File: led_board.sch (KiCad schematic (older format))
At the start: 12 parts, among them J1 Conn_Coaxial, J2 Conn_Coaxial, J3 Conn_Coaxial, J4 Conn_Coaxial

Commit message: edits
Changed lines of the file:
@@
 Wire Wire Line
 	3000 3200 1500 3200
+$Comp
+L power:GND #PWR?
+U 1 1 5E6218D4
+P 3850 1950
+F 0 "#PWR?" H 3850 1700 50  0001 C CNN
+F 1 "GND" H 3855 1777 50  0000 C CNN
+F 2 "" H 3850 1950 50  0001 C CNN
+F 3 "" H 3850 1950 50  0001 C CNN
+	1    3850 1950
+	1    0    0    -1
+$EndComp
+Wire Wire Line
+	3850 1950 3850 1750
+Wire Wire Line
+	3850 1750 4000 1750
+Wire Wire Line
+	4000 1750 4000 1950
+Wire Wire Line
+	4000 1950 3850 1950
+Connection ~ 3850 1950
 $EndSCHEMATC

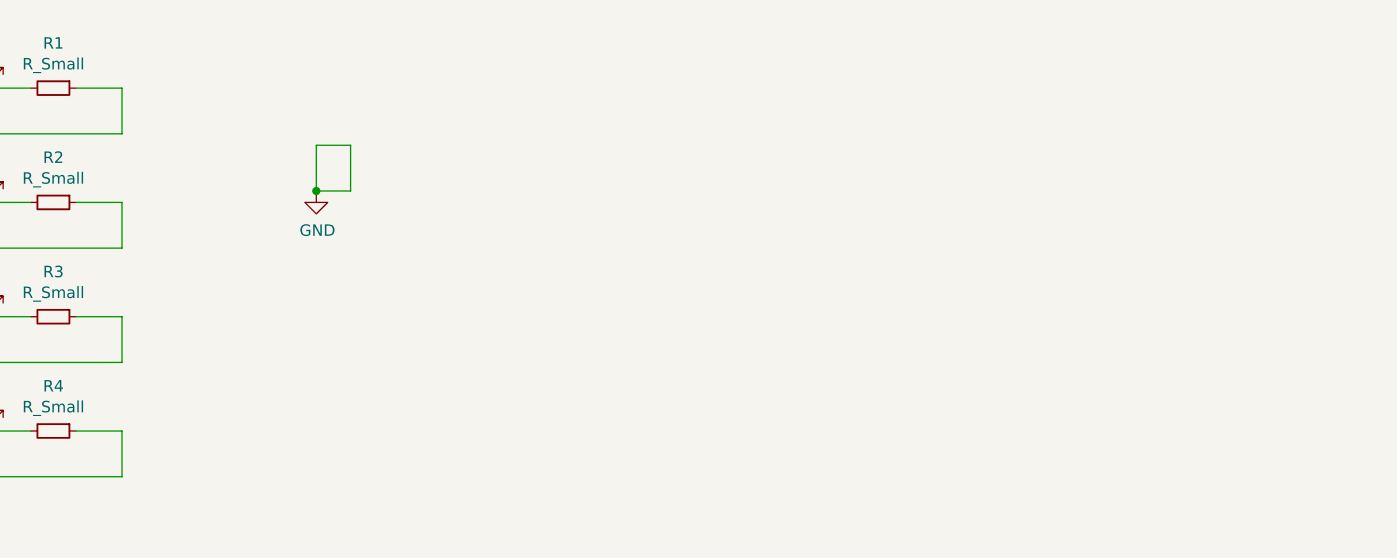
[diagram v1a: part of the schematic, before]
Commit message: rework for thorlabs 30mm cage
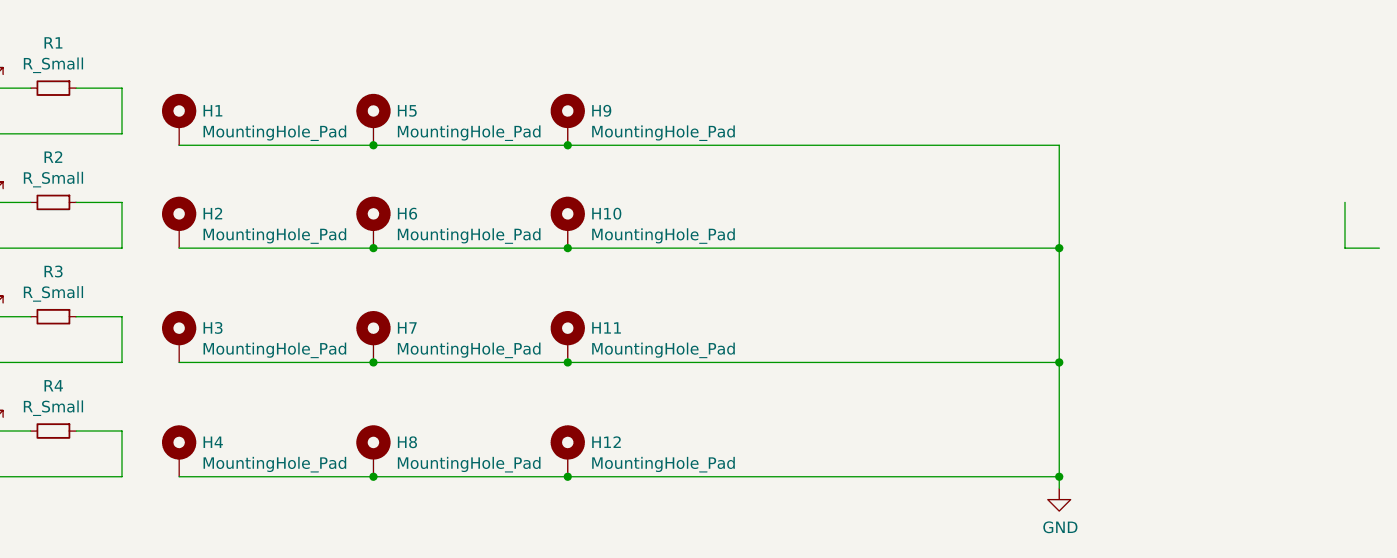
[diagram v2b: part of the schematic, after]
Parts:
- added H1, H10, H11, H12, H2, H3, H4, H5, H6, H7, H8, H9: MountingHole_Pad, MountingHole:MountingHole_6mm_Pad_Via, symbol Mechanical:MountingHole_Pad
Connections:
- wire segments 24 -> 38
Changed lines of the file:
@@
 	3000 3200 1500 3200
 $Comp
-L power:GND #PWR?
+L power:GND #PWR0101
 U 1 1 5E6218D4
-P 3850 1950
-F 0 "#PWR?" H 3850 1700 50  0001 C CNN
-F 1 "GND" H 3855 1777 50  0000 C CNN
-F 2 "" H 3850 1950 50  0001 C CNN
-F 3 "" H 3850 1950 50  0001 C CNN
-	1    3850 1950
+P 7100 3250
+F 0 "#PWR0101" H 7100 3000 50  0001 C CNN
+F 1 "GND" H 7105 3077 50  0000 C CNN
+F 2 "" H 7100 3250 50  0001 C CNN
+F 3 "" H 7100 3250 50  0001 C CNN
+	1    7100 3250
 	1    0    0    -1
 $EndComp
 Wire Wire Line
-	3850 1950 3850 1750
+	8350 2200 8350 2000
 Wire Wire Line
-	3850 1750 4000 1750
+	8500 2200 8350 2200
+$Comp
+L Mechanical:MountingHole_Pad H1
+U 1 1 5E61B0AD
+P 3250 1650
+F 0 "H1" H 3350 1699 50  0000 L CNN
+F 1 "MountingHole_Pad" H 3350 1608 50  0000 L CNN
+F 2 "MountingHole:MountingHole_6mm_Pad_Via" H 3250 1650 50  0001 C CNN
+F 3 "~" H 3250 1650 50  0001 C CNN
+	1    3250 1650
+	1    0    0    -1
+$EndComp
+$Comp
+L Mechanical:MountingHole_Pad H5
+U 1 1 5E61C87A
+P 4100 1650
+F 0 "H5" H 4200 1699 50  0000 L CNN
+F 1 "MountingHole_Pad" H 4200 1608 50  0000 L CNN
+F 2 "MountingHole:MountingHole_6mm_Pad_Via" H 4100 1650 50  0001 C CNN
+F 3 "~" H 4100 1650 50  0001 C CNN
+	1    4100 1650
+	1    0    0    -1
+$EndComp
+$Comp
+L Mechanical:MountingHole_Pad H9
+U 1 1 5E61CDCB
+P 4950 1650
+F 0 "H9" H 5050 1699 50  0000 L CNN
+F 1 "MountingHole_Pad" H 5050 1608 50  0000 L CNN
+F 2 "MountingHole:MountingHole_6mm_Pad_Via" H 4950 1650 50  0001 C CNN
+F 3 "~" H 4950 1650 50  0001 C CNN
+	1    4950 1650
+	1    0    0    -1
+$EndComp
+$Comp
+L Mechanical:MountingHole_Pad H2
+U 1 1 5E627D57
+P 3250 2100
+F 0 "H2" H 3350 2149 50  0000 L CNN
+F 1 "MountingHole_Pad" H 3350 2058 50  0000 L CNN
+F 2 "MountingHole:MountingHole_6mm_Pad_Via" H 3250 2100 50  0001 C CNN
+F 3 "~" H 3250 2100 50  0001 C CNN
+	1    3250 2100
+	1    0    0    -1
+$EndComp
+$Comp
+L Mechanical:MountingHole_Pad H6
+U 1 1 5E627D5D
+P 4100 2100
+F 0 "H6" H 4200 2149 50  0000 L CNN
+F 1 "MountingHole_Pad" H 4200 2058 50  0000 L CNN
+F 2 "MountingHole:MountingHole_6mm_Pad_Via" H 4100 2100 50  0001 C CNN
+F 3 "~" H 4100 2100 50  0001 C CNN
+	1    4100 2100
+	1    0    0    -1
+$EndComp
+$Comp
+L Mechanical:MountingHole_Pad H10
+U 1 1 5E627D63
+P 4950 2100
+F 0 "H10" H 5050 2149 50  0000 L CNN
+F 1 "MountingHole_Pad" H 5050 2058 50  0000 L CNN
+F 2 "MountingHole:MountingHole_6mm_Pad_Via" H 4950 2100 50  0001 C CNN
+F 3 "~" H 4950 2100 50  0001 C CNN
+	1    4950 2100
+	1    0    0    -1
+$EndComp
+$Comp
+L Mechanical:MountingHole_Pad H3
+U 1 1 5E628ADF
+P 3250 2600
+F 0 "H3" H 3350 2649 50  0000 L CNN
+F 1 "MountingHole_Pad" H 3350 2558 50  0000 L CNN
+F 2 "MountingHole:MountingHole_6mm_Pad_Via" H 3250 2600 50  0001 C CNN
+F 3 "~" H 3250 2600 50  0001 C CNN
+	1    3250 2600
+	1    0    0    -1
+$EndComp
+$Comp
+L Mechanical:MountingHole_Pad H7
+U 1 1 5E628AE5
+P 4100 2600
+F 0 "H7" H 4200 2649 50  0000 L CNN
+F 1 "MountingHole_Pad" H 4200 2558 50  0000 L CNN
+F 2 "MountingHole:MountingHole_6mm_Pad_Via" H 4100 2600 50  0001 C CNN
+F 3 "~" H 4100 2600 50  0001 C CNN
+	1    4100 2600
+	1    0    0    -1
+$EndComp
+$Comp
+L Mechanical:MountingHole_Pad H11
+U 1 1 5E628AEB
+P 4950 2600
+F 0 "H11" H 5050 2649 50  0000 L CNN
+F 1 "MountingHole_Pad" H 5050 2558 50  0000 L CNN
+F 2 "MountingHole:MountingHole_6mm_Pad_Via" H 4950 2600 50  0001 C CNN
+F 3 "~" H 4950 2600 50  0001 C CNN
+	1    4950 2600
+	1    0    0    -1
+$EndComp
+$Comp
+L Mechanical:MountingHole_Pad H4
+U 1 1 5E62CA13
+P 3250 3100
+F 0 "H4" H 3350 3149 50  0000 L CNN
+F 1 "MountingHole_Pad" H 3350 3058 50  0000 L CNN
+F 2 "MountingHole:MountingHole_6mm_Pad_Via" H 3250 3100 50  0001 C CNN
+F 3 "~" H 3250 3100 50  0001 C CNN
+	1    3250 3100
+	1    0    0    -1
+$EndComp
+$Comp
+L Mechanical:MountingHole_Pad H8
+U 1 1 5E62CA19
+P 4100 3100
+F 0 "H8" H 4200 3149 50  0000 L CNN
+F 1 "MountingHole_Pad" H 4200 3058 50  0000 L CNN
+F 2 "MountingHole:MountingHole_6mm_Pad_Via" H 4100 3100 50  0001 C CNN
+F 3 "~" H 4100 3100 50  0001 C CNN
+	1    4100 3100
+	1    0    0    -1
+$EndComp
+$Comp
+L Mechanical:MountingHole_Pad H12
+U 1 1 5E62CA1F
+P 4950 3100
+F 0 "H12" H 5050 3149 50  0000 L CNN
+F 1 "MountingHole_Pad" H 5050 3058 50  0000 L CNN
+F 2 "MountingHole:MountingHole_6mm_Pad_Via" H 4950 3100 50  0001 C CNN
+F 3 "~" H 4950 3100 50  0001 C CNN
+	1    4950 3100
+	1    0    0    -1
+$EndComp
 Wire Wire Line
-	4000 1750 4000 1950
+	3250 3200 4100 3200
 Wire Wire Line
-	4000 1950 3850 1950
-Connection ~ 3850 1950
+	7100 3200 7100 3250
+Connection ~ 4100 3200
+Wire Wire Line
+	4100 3200 4950 3200
+Connection ~ 4950 3200
+Wire Wire Line
+	3250 2700 4100 2700
+Wire Wire Line
+	7100 2700 7100 3200
+Connection ~ 4100 2700
+Wire Wire Line
+	4100 2700 4950 2700
+Connection ~ 4950 2700
+Connection ~ 7100 3200
+Wire Wire Line
+	3250 2200 4100 2200
+Wire Wire Line
+	7100 2200 7100 2700
+Connection ~ 4100 2200
+Wire Wire Line
+	4100 2200 4950 2200
+Connection ~ 4950 2200
+Connection ~ 7100 2700
+Wire Wire Line
+	3250 1750 4100 1750
+Wire Wire Line
+	7100 1750 7100 2200
+Connection ~ 4100 1750
+Wire Wire Line
+	4100 1750 4950 1750
+Connection ~ 4950 1750
+Connection ~ 7100 2200
+Wire Wire Line
+	4950 1750 7100 1750
+Wire Wire Line
+	4950 2200 7100 2200
+Wire Wire Line
+	4950 2700 7100 2700
+Wire Wire Line
+	4950 3200 7100 3200
 $EndSCHEMATC

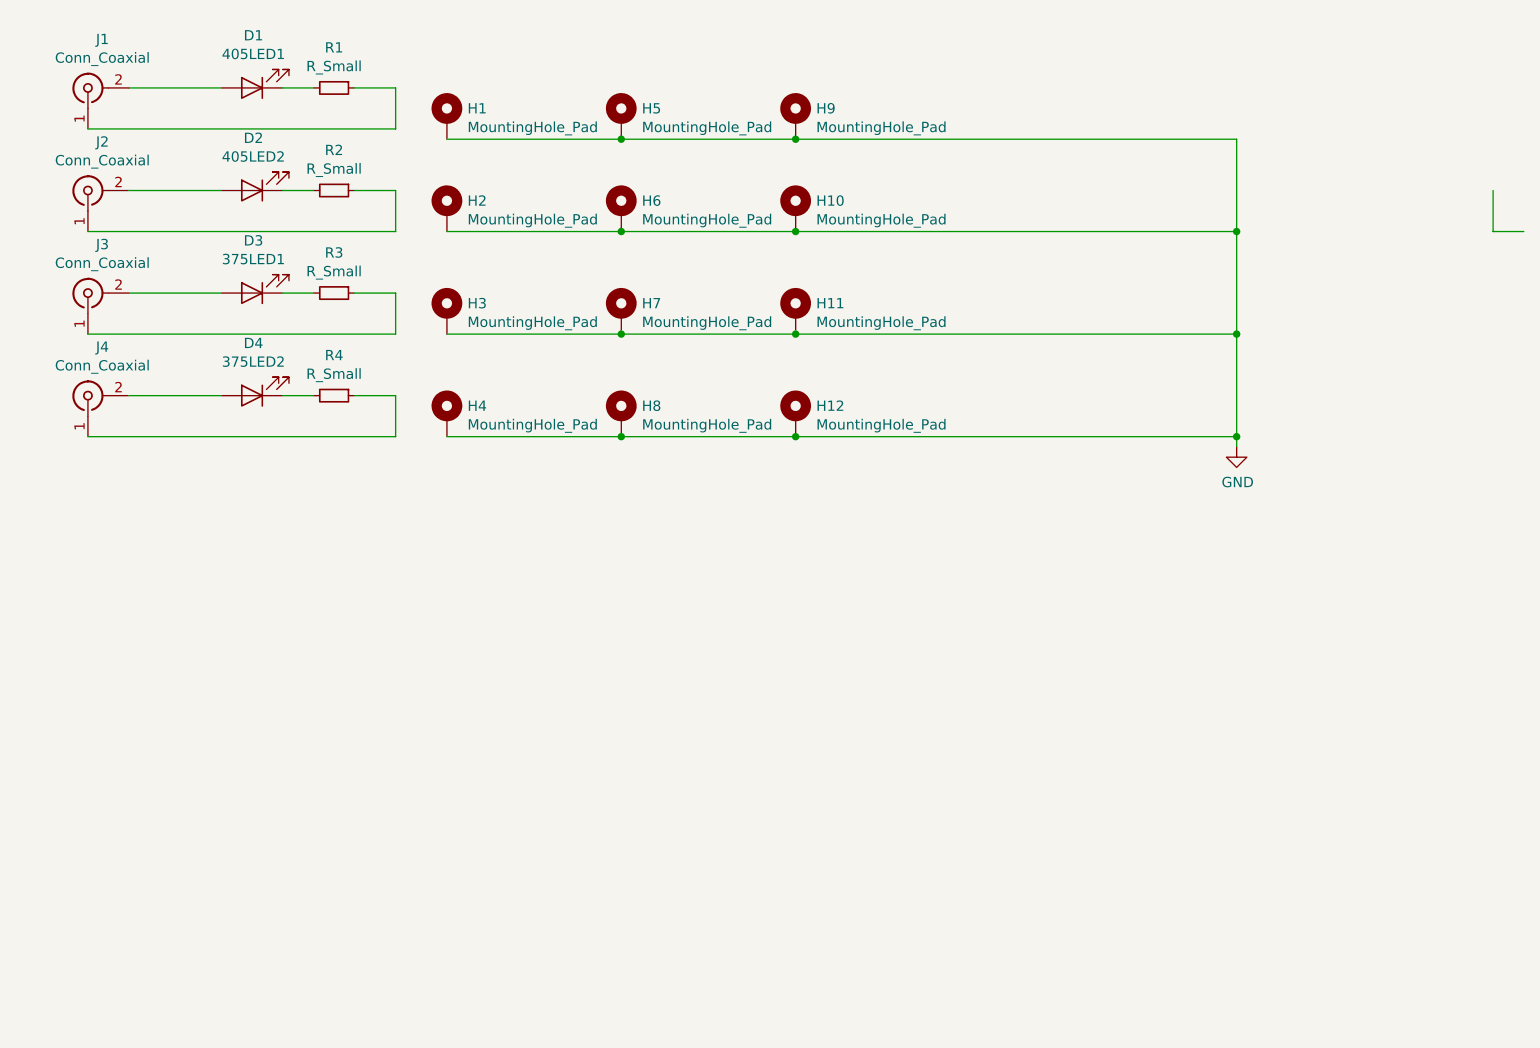
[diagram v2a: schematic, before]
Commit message: no res term boards added, net class updated
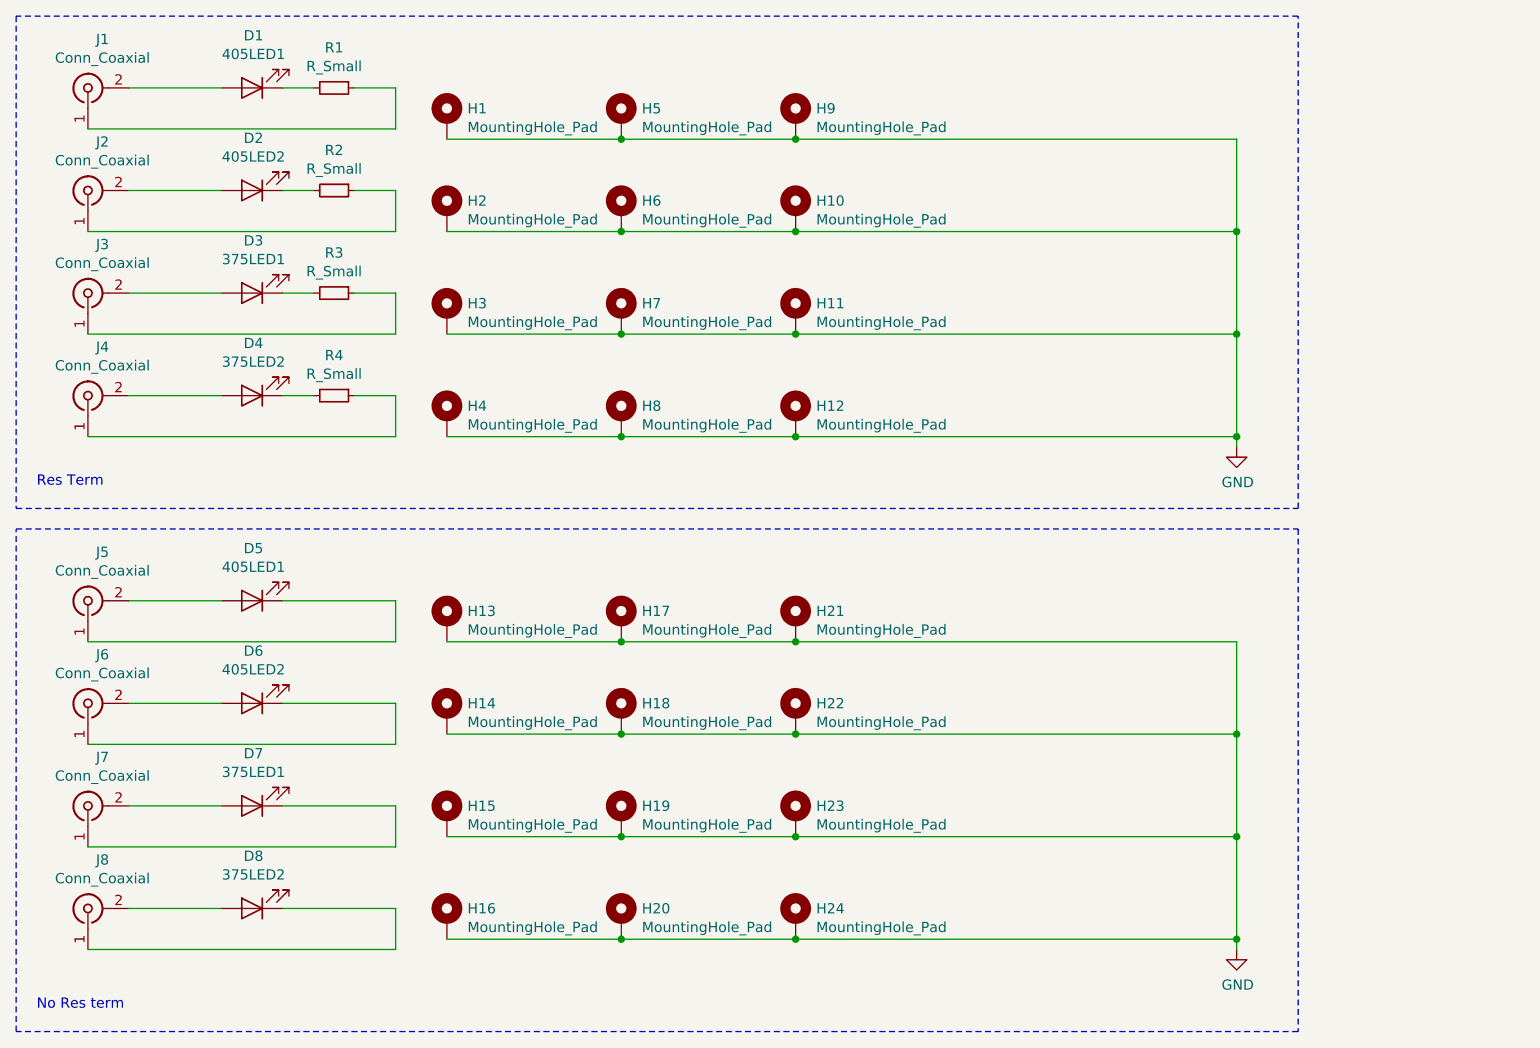
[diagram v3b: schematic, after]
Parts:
- added D5: 405LED1, LED_SMD:LED_0603_1608Metric_Pad1.05x0.95mm_HandSolder, symbol Device:LED
- added D6: 405LED2, LED_SMD:LED_1206_3216Metric_Pad1.42x1.75mm_HandSolder, symbol Device:LED
- added D7: 375LED1, leds:LED_SMD_Kingbright_405_2012, symbol Device:LED
- added D8: 375LED2, leds:LED_SMD_Vishay_405_16, symbol Device:LED
- added H13, H14, H15, H16, H17, H18, H19, H20, H21, H22, H23, H24: MountingHole_Pad, MountingHole:MountingHole_6mm_Pad_Via, symbol Mechanical:MountingHole_Pad
- added J5, J6, J7, J8: Conn_Coaxial, Connector_Coaxial:SMA_Amphenol_132289_EdgeMount, symbol Connector:Conn_Coaxial
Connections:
- wire segments 38 -> 68
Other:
- note added: "No Res term"
- note added: "Res Term"

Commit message: Fixed a big dumb. nearly done.
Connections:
- net GND: now also D5.1 (K), D6.1 (K), D7.1 (K), D8.1 (K), J1.2 (Ext), J2.2 (Ext), J3.2 (Ext), J4.2 (Ext), J5.2 (Ext), J6.2 (Ext), J7.2 (Ext), J8.2 (Ext), R1.1, R2.1, R3.1, R4.1
- net at J1.1 (In): now also D1.2 (A); no longer R1.1
- net at J2.1 (In): now also D2.2 (A); no longer R2.1
- net at J3.1 (In): now also D3.2 (A); no longer R3.1
- net at J4.1 (In): now also D4.2 (A); no longer R4.1
- net at J5.1 (In): now also D5.2 (A); no longer D5.1 (K)
- net at J6.1 (In): now also D6.2 (A); no longer D6.1 (K)
- net at J7.1 (In): now also D7.2 (A); no longer D7.1 (K)
- net at J8.1 (In): now also D8.2 (A); no longer D8.1 (K)
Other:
- moved on the sheet: H1, H14, H15, H16, H18, H19, H20, H22, H23, H24, H5, H9
